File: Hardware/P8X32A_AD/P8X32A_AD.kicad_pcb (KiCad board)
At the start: 4 copper layers, 42 x 50 mm, 24 parts, among them J1 Conn_01x12, J2 Conn_01x12, J3 Conn_01x08, J4 Conn_01x07, SW1 SW_PUSH, U1 Propeller, U2 24LC512, U3 AD7812, Y1 5Mhz

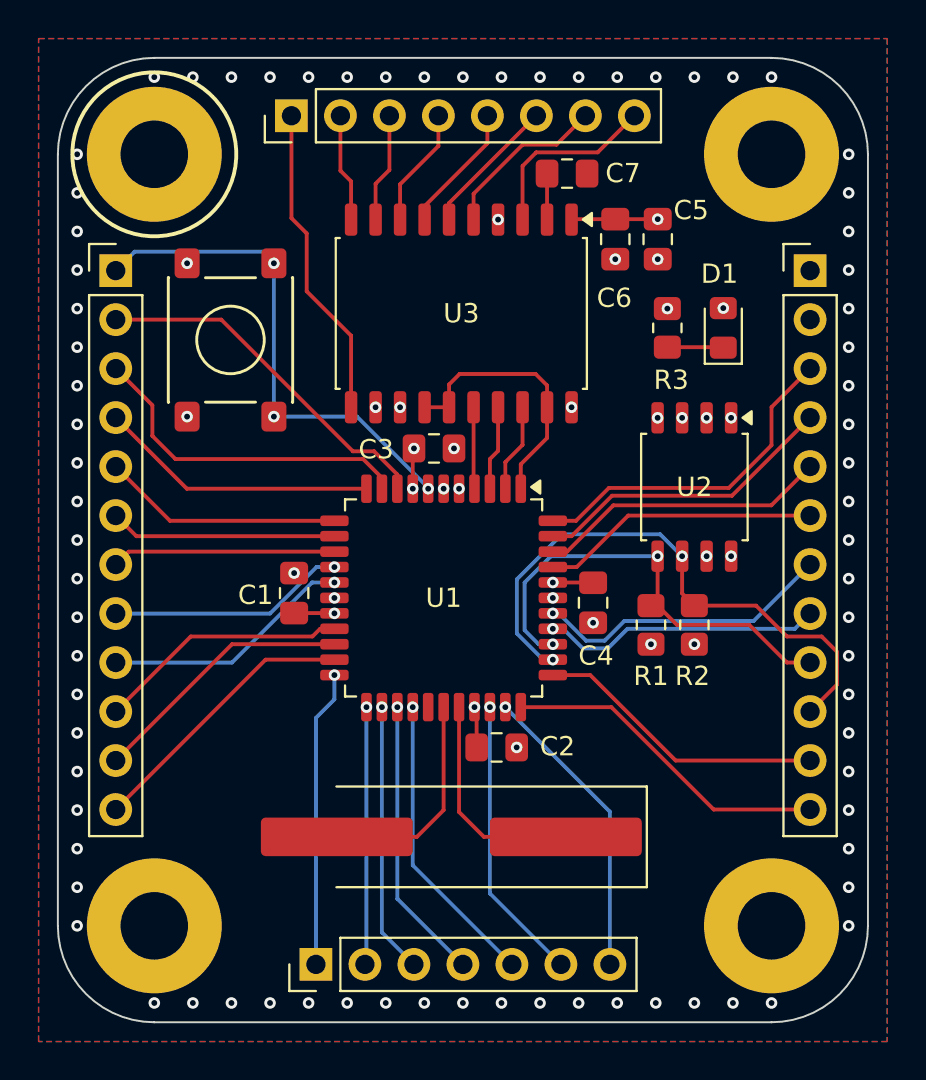
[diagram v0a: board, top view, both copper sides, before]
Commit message: Hardware updates. Add Lr04 lora module datasheets
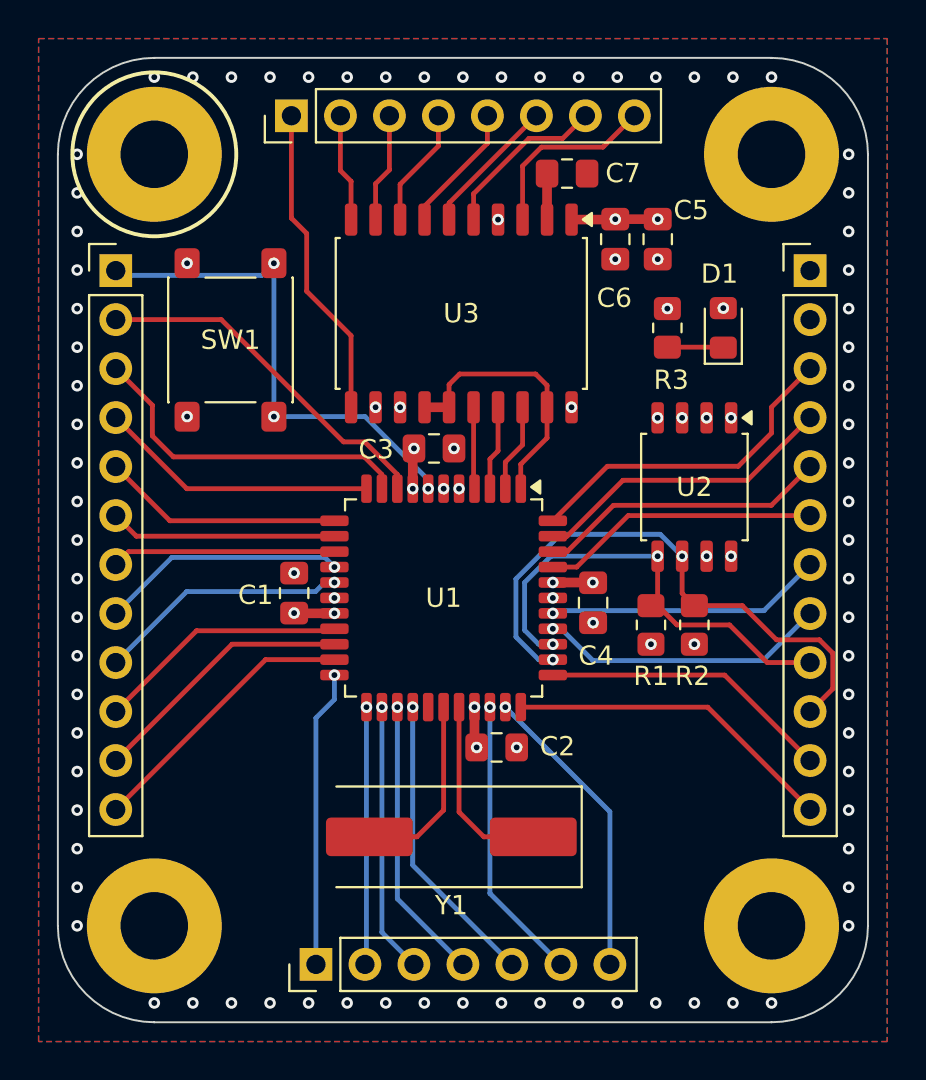
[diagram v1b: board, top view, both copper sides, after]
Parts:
- SW1: footprint General:SW_SPST -> Button_Switch_SMD:SW_SPST_PTS645Sx43SMTR92
- Y1: footprint Crystal:Crystal_SMD_HC49-SD_HandSoldering -> Crystal:Crystal_SMD_HC49-SD
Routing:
- net RX: track 15.6 -> 14.4 mm
- net TX: track 14.5 -> 15.0 mm
- net +3.3V: vias 11 -> 15
